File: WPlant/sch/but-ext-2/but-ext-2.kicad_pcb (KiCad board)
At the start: 2 copper layers, 149 x 19 mm, 15 parts, among them J1 eInk, J4 But2, SW1 SW_Push, SW2 SW_Push, SW3 SW_Push, SW4 SW_Push, U2 SMTSOM365BTR, U3 SMTSOM365BTR

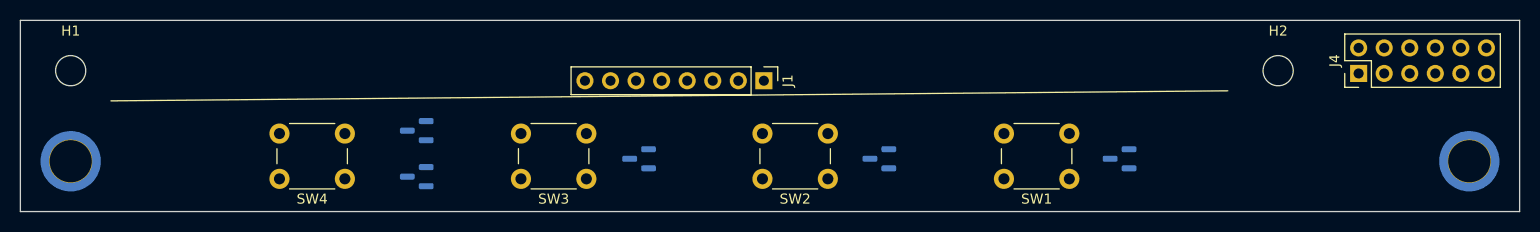
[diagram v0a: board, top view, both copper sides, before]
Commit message: One of Buttons PCB roughted
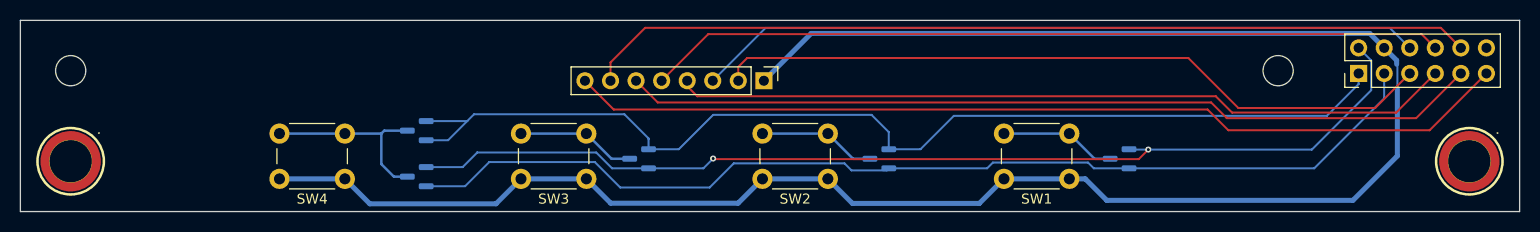
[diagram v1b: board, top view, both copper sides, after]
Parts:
- U2, U3: moved to F.Cu
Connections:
- D4 pad 1: /W3 -> /W2
- D4 pad 2: /W2 -> /W3
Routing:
- net /GND: track 0.00 -> 195.4 mm
- net /W1: track 0.00 -> 107.5 mm
- net /W2: track 0.00 -> 105.1 mm, vias 0 -> 2
- net /W3: track 0.00 -> 104.5 mm
- net Net-(J1-Pin_8): track 0.00 -> 94.0 mm
- net Net-(J1-Pin_7): track 0.00 -> 88.6 mm
- net Net-(J1-Pin_6): track 0.00 -> 85.4 mm
- net Net-(J1-Pin_5): track 0.00 -> 79.4 mm
- net Net-(J1-Pin_4): track 0.00 -> 77.6 mm
- net Net-(J1-Pin_3): track 0.00 -> 72.3 mm
- net Net-(J1-Pin_2): track 0.00 -> 72.0 mm
- net Net-(D4-Pad3): track 0.00 -> 19.0 mm
- net Net-(D3-Pad3): track 0.00 -> 11.8 mm
- net Net-(D2-Pad3): track 0.00 -> 11.7 mm
- net Net-(D1-Pad3): track 0.00 -> 11.6 mm

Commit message: Add 3D model of Robots head pole support
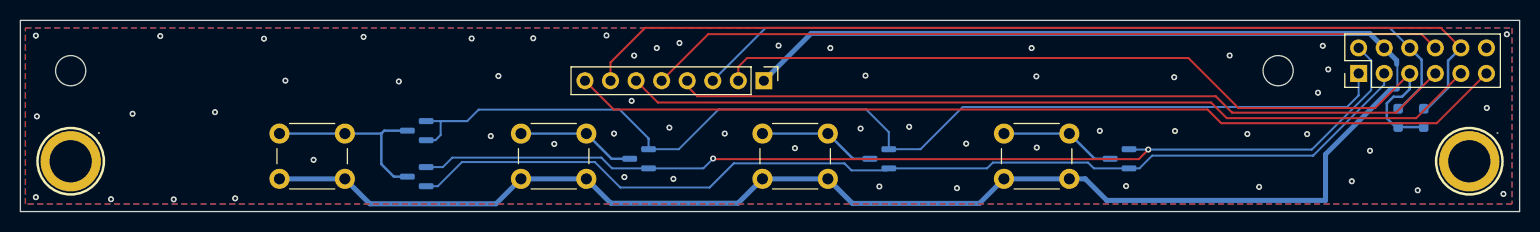
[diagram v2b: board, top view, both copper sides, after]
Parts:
- added R1: 100K, Resistor_SMD:R_0603_1608Metric_Pad0.98x0.95mm_HandSolder, B.Cu at (201.9, 59.7)
- added R2: 100K, Resistor_SMD:R_0603_1608Metric_Pad0.98x0.95mm_HandSolder, B.Cu at (204.5, 59.7)
- U2, U3: footprint easyeda2kicad:SMD_BD5.6-D4.1 -> but:SMD_BD5.6-D4.1
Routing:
- net Net-(J1-Pin_2): track 72.0 -> 81.9 mm
- net Net-(J1-Pin_7): track 88.6 -> 96.3 mm
- net Net-(J1-Pin_3): track 72.3 -> 79.9 mm
- net /W1: track 107.5 -> 109.8 mm
- net /GND: track 195.4 -> 194.2 mm, vias 0 -> 58
- net /W3: track 104.5 -> 103.6 mm
- net Net-(J1-Pin_8): track 94.0 -> 93.4 mm
- added copper zone on B.Cu, net /GND
- added copper zone on F.Cu, net /GND
